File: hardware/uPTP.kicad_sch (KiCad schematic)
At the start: 20 parts, among them J1 Conn_01x04_Pin, J2 PPS_UFL, J3 PPS_SMA, J5 AUX_PWR, U1 CH32V307WCU6, Y1 Crystal_GND2_Small

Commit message: Done for the day
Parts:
- J1: value Conn_01x04_Pin -> UART_HDR
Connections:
- net GND: now also J1.1 (Pin_1), J5.1 (Pin_1), U1.0 (EP), U1.12 (VSSA), U1.18 (VSS), U1.49 (VSS), U1.69 (VSS)
- net Power/V_AUX: now also J5.2 (Pin_2)
- net UART_TX: now reaches J1.2 (Pin_2)
- net UART_RX: now reaches J1.3 (Pin_3)
- net +3V3: now reaches J1.4 (Pin_4)
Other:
- moved on the sheet: J1, J5

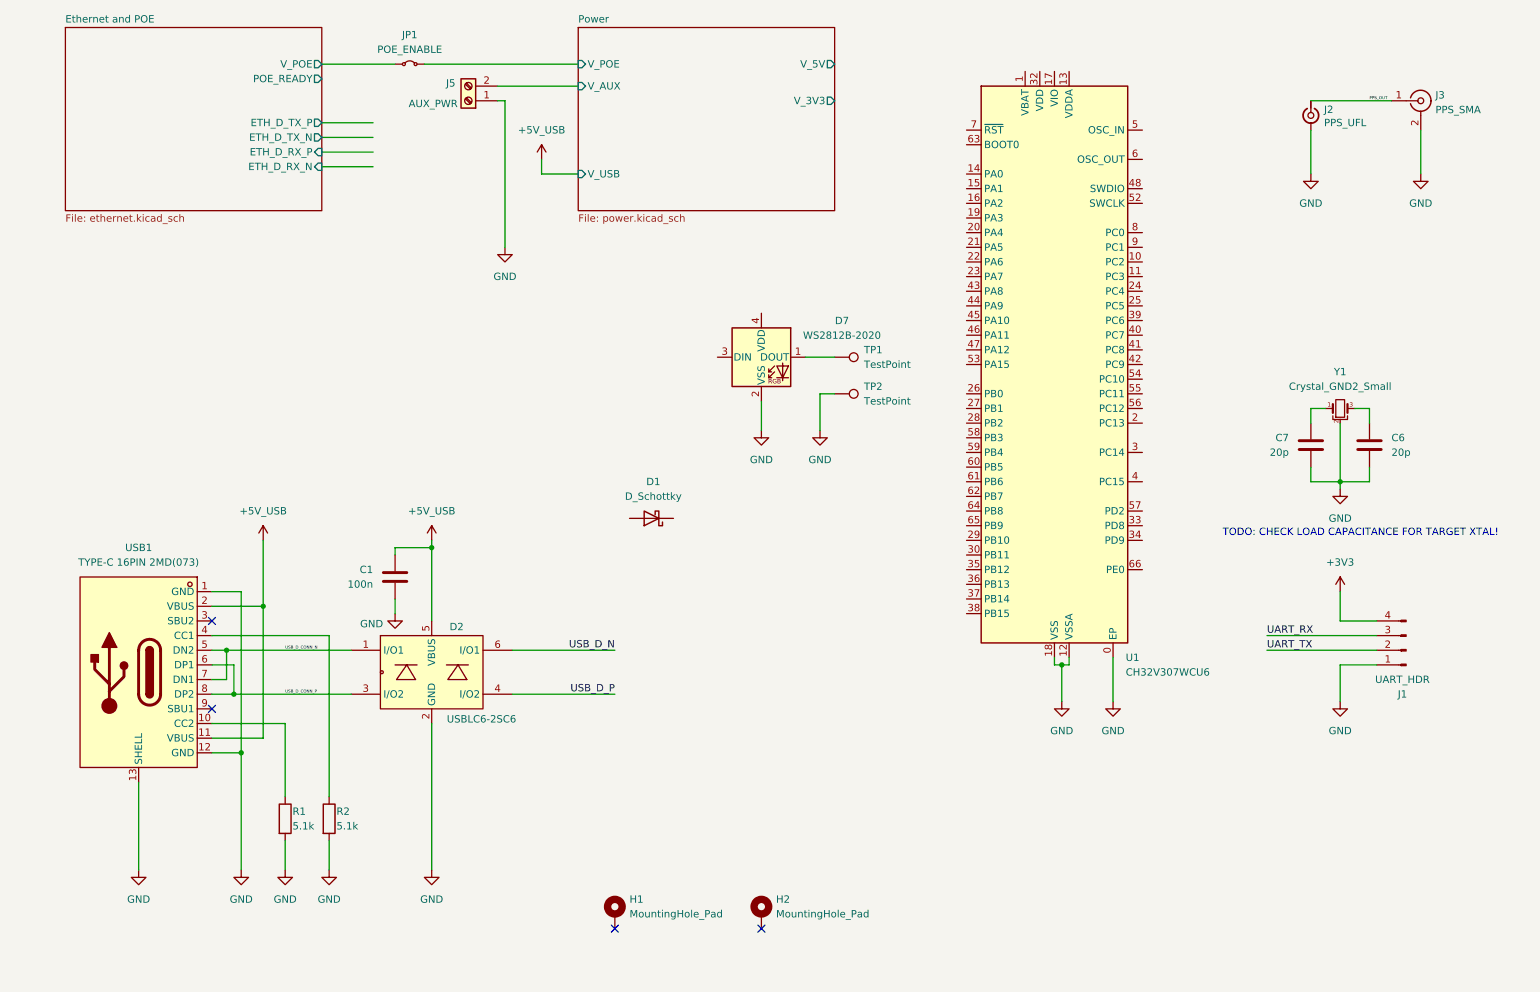
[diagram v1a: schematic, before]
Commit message: Prep for change to SI3404 https://www.skyworksinc.com/-/media/Skyworks/SL/documents/public/application-notes/an1130-si3404-06x-dg.pdf
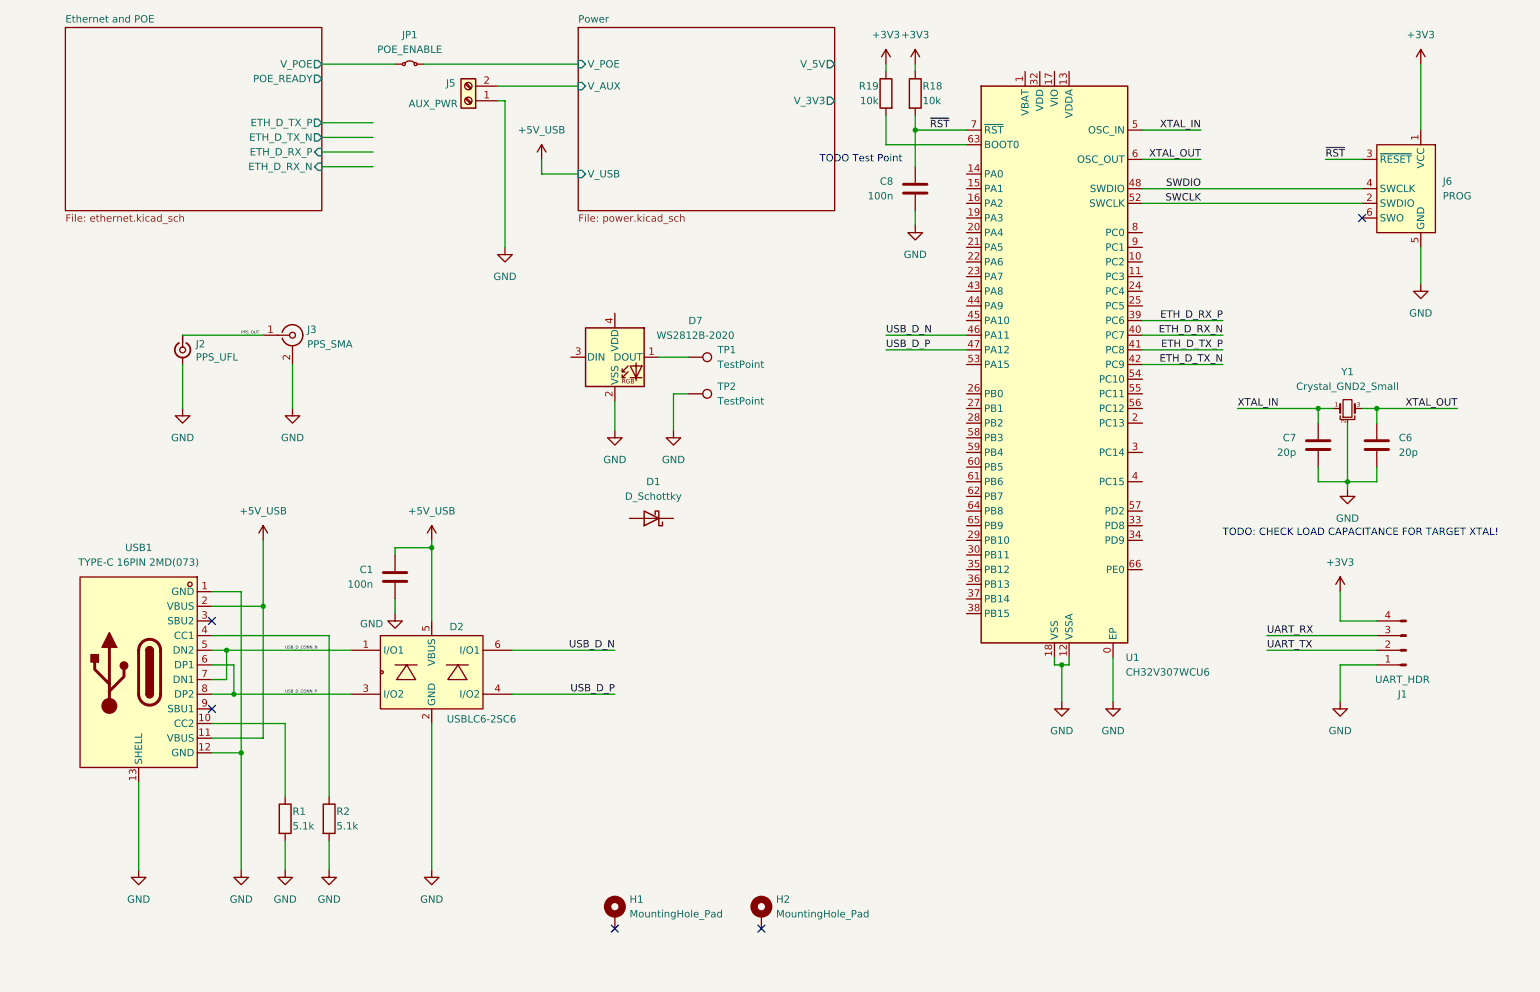
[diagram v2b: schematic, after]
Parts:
- added C8: 100n, Capacitor_SMD:C_0402_1005Metric, symbol Device:C
- added J6: PROG, Connector:Tag-Connect_TC2030-IDC-NL_2x03_P1.27mm_Vertical, symbol Connector:Conn_ARM_SWD_TagConnect_TC2030-NL
- added R18, R19: 10k, Resistor_SMD:R_0402_1005Metric, symbol Device:R
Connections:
- net +3V3: now also J6.1 (VCC), R18.1, R19.1
- net GND: now also C8.2, J6.5 (GND)
- net USB_D_N: now also U1.46 (PA11)
- net USB_D_P: now also U1.47 (PA12)
- net XTAL_OUT: now reaches C6.1, Y1.3
- net XTAL_OUT: now also U1.6 (OSC_OUT)
- net XTAL_IN: now reaches C7.1, Y1.1
- net XTAL_IN: now also U1.5 (OSC_IN)
- net ETH_D_RX_P: now reaches U1.39 (PC6)
- net ETH_D_RX_N: now reaches U1.40 (PC7)
- net ETH_D_TX_P: now reaches U1.41 (PC8)
- net ETH_D_TX_N: now reaches U1.42 (PC9)
- net SWDIO: now reaches U1.48 (SWDIO)
- net SWDIO: now also J6.4 (SWCLK)
- net SWCLK: now reaches U1.52 (SWCLK)
- net SWCLK: now also J6.2 (SWDIO)
- net at U1.63 (BOOT0): now also R19.2
- net ~{RST}: now reaches U1.7 (~{RST})
- net ~{RST}: now also C8.1, J6.3 (~{RESET}), R18.2
- no-connect marks 4 -> 5
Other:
- note added: "TODO Test Point"
- moved on the sheet: C6, C7, D7, J2, J3, TP1, TP2, Y1

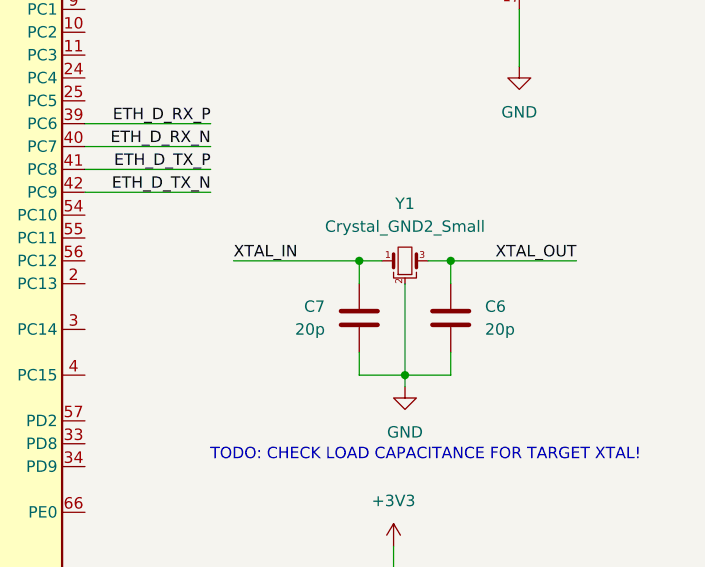
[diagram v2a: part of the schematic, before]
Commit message: Add XTAL, rough POE Schematic
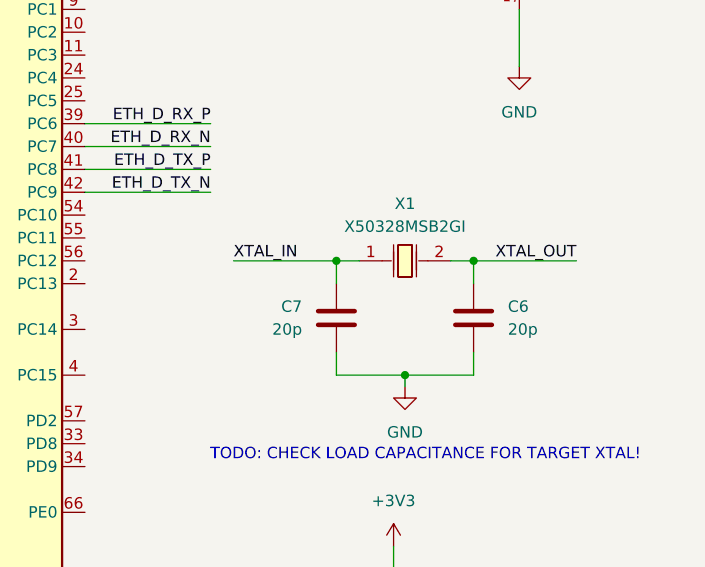
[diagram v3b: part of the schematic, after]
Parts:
- removed Y1: Crystal_GND2_Small, symbol Device:Crystal_GND2_Small
- added X1: X50328MSB2GI, uPTP:CRYSTAL-SMD_L5.0-W3.2, symbol uPTP:X50328MSB2GI
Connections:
- net XTAL_IN: now also X1.1
- net XTAL_OUT: now also X1.2
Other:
- moved on the sheet: C6, C7
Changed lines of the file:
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@@
-	)
-	(junction
-		(at 259.08 97.79)
-		(diameter 0)
-		(color 0 0 0 0)
 	)
 	(junction
@@
 	)
 	(junction
-		(at 248.92 97.79)
+		(at 261.62 97.79)
+		(diameter 0)
+		(color 0 0 0 0)
+	)
+	(junction
+		(at 246.38 97.79)
 		(diameter 0)
 		(color 0 0 0 0)
@@
 	(wire
 		(pts
-			(xy 254 110.49) (xy 248.92 110.49)
+			(xy 254 110.49) (xy 246.38 110.49)
+		)
+		(stroke
+			(width 0)
+			(type default)
+		)
+	)
+	(wire
+		(pts
+			(xy 246.38 97.79) (xy 248.92 97.79)
 		)
 		(stroke
@@
 	(wire
 		(pts
+			(xy 261.62 97.79) (xy 273.05 97.79)
+		)
+		(stroke
+			(width 0)
+			(type default)
+		)
+	)
+	(wire
+		(pts
 			(xy 179.07 63.5) (xy 179.07 66.04)
 		)
@@
 	(wire
 		(pts
-			(xy 259.08 110.49) (xy 254 110.49)
+			(xy 261.62 110.49) (xy 254 110.49)
 		)
 		(stroke
@@
 	(wire
 		(pts
+			(xy 259.08 97.79) (xy 261.62 97.79)
+		)
+		(stroke
+			(width 0)
+			(type default)
+		)
+	)
+	(wire
+		(pts
 			(xy 106.68 41.91) (xy 120.65 41.91)
 		)
@@
 	(wire
 		(pts
-			(xy 248.92 97.79) (xy 248.92 100.33)
+			(xy 246.38 97.79) (xy 246.38 100.33)
 		)
 		(stroke
@@
 	(wire
 		(pts
-			(xy 254 100.33) (xy 254 110.49)
-		)
-		(stroke
-			(width 0)
-			(type default)
-		)
-	)
-	(wire
-		(pts
 			(xy 57.15 129.54) (xy 62.23 129.54)
 		)
@@
 	(wire
 		(pts
-			(xy 259.08 97.79) (xy 273.05 97.79)
-		)
-		(stroke
-			(width 0)
-			(type default)
-		)
-	)
-	(wire
-		(pts
 			(xy 59.69 139.7) (xy 59.69 144.78)
 		)
@@
 	(wire
 		(pts
-			(xy 256.54 97.79) (xy 259.08 97.79)
-		)
-		(stroke
-			(width 0)
-			(type default)
-		)
-	)
-	(wire
-		(pts
 			(xy 218.44 85.09) (xy 232.41 85.09)
 		)
@@
 	(wire
 		(pts
-			(xy 234.95 97.79) (xy 248.92 97.79)
+			(xy 234.95 97.79) (xy 246.38 97.79)
 		)
 		(stroke
@@
 	(wire
 		(pts
-			(xy 259.08 107.95) (xy 259.08 110.49)
-		)
-		(stroke
-			(width 0)
-			(type default)
-		)
-	)
-	(wire
-		(pts
-			(xy 251.46 97.79) (xy 248.92 97.79)
+			(xy 261.62 107.95) (xy 261.62 110.49)
 		)
 		(stroke
@@
 	(wire
 		(pts
-			(xy 259.08 100.33) (xy 259.08 97.79)
+			(xy 261.62 100.33) (xy 261.62 97.79)
 		)
 		(stroke
@@
 	(wire
 		(pts
-			(xy 248.92 110.49) (xy 248.92 107.95)
+			(xy 246.38 110.49) (xy 246.38 107.95)
 		)
 		(stroke
@@
 	(symbol
 		(lib_id "Device:C")
-		(at 259.08 104.14 0)
+		(at 261.62 104.14 0)
 		(unit 1)
 		(exclude_from_sim no)
@@
 		(dnp no)
 		(property "Reference" "C6"
-			(at 262.89 102.8699 0)
+			(at 265.43 102.8699 0)
 			(effects
 				(font
@@
 		)
 		(property "Value" "20p"
-			(at 262.89 105.4099 0)
+			(at 265.43 105.4099 0)
 			(effects
 				(font
@@
 		)
 		(property "Footprint" "Capacitor_SMD:C_0402_1005Metric"
-			(at 260.0452 107.95 0)
+			(at 262.5852 107.95 0)
 			(effects
 				(font
@@
 		)
 		(property "Datasheet" "~"
-			(at 259.08 104.14 0)
+			(at 261.62 104.14 0)
 			(effects
 				(font
@@
 		)
 		(property "Description" "Unpolarized capacitor"
-			(at 259.08 104.14 0)
+			(at 261.62 104.14 0)
 			(effects
 				(font
@@
 	)
 	(symbol
-		(lib_id "Device:Crystal_GND2_Small")
-		(at 254 97.79 0)
-		(unit 1)
-		(exclude_from_sim no)
-		(in_bom yes)
-		(on_board yes)
-		(dnp no)
-		(fields_autoplaced yes)
-		(property "Reference" "Y1"
-			(at 254 91.44 0)
-			(effects
-				(font
-					(size 1.27 1.27)
-				)
-			)
-		)
-		(property "Value" "Crystal_GND2_Small"
-			(at 254 93.98 0)
-			(effects
-				(font
-					(size 1.27 1.27)
-				)
-			)
-		)
-		(property "Footprint" ""
-			(at 254 97.79 0)
-			(effects
-				(font
-					(size 1.27 1.27)
-				)
-				(hide yes)
-			)
-		)
-		(property "Datasheet" "~"
-			(at 254 97.79 0)
-			(effects
-				(font
-					(size 1.27 1.27)
-				)
-				(hide yes)
-			)
-		)
-		(property "Description" "Three pin crystal, GND on pin 2, small symbol"
-			(at 254 97.79 0)
-			(effects
-				(font
-					(size 1.27 1.27)
-				)
-				(hide yes)
-			)
-		)
-		(pin "2"
-		)
-		(pin "3"
-		)
-		(pin "1"
-		)
-		(instances
-			(project ""
-				(path "/c29659fd-9e8d-4714-a690-4e74e6e849c2"
-					(reference "Y1")
-					(unit 1)
-				)
-			)
-		)
-	)
-	(symbol
 		(lib_id "Device:C")
 		(at 179.07 59.69 0)
@@
 	)
 	(symbol
+		(lib_id "uPTP:X50328MSB2GI")
+		(at 254 97.79 0)
+		(unit 1)
+		(exclude_from_sim no)
+		(in_bom yes)
+		(on_board yes)
+		(dnp no)
+		(fields_autoplaced yes)
+		(property "Reference" "X1"
+			(at 254 91.44 0)
+			(effects
+				(font
+					(size 1.27 1.27)
+				)
+			)
+		)
+		(property "Value" "X50328MSB2GI"
+			(at 254 93.98 0)
+			(effects
+				(font
+					(size 1.27 1.27)
+				)
+			)
+		)
+		(property "Footprint" "uPTP:CRYSTAL-SMD_L5.0-W3.2"
+			(at 254 105.41 0)
+			(effects
+				(font
+					(size 1.27 1.27)
+				)
+				(hide yes)
+			)
+		)
+		(property "Datasheet" "https://lcsc.com/product-detail/SMD-Crystals_YSX530GA-8MHZ-20PF-10PPM-40-85_C115962.html"
+			(at 254 107.95 0)
+			(effects
+				(font
+					(size 1.27 1.27)
+				)
+				(hide yes)
+			)
+		)
+		(property "Description" "8MHz Crystal Oscillator (Basic Part)"
+			(at 255.27 112.776 0)
+			(effects
+				(font
+					(size 1.27 1.27)
+				)
+				(hide yes)
+			)
+		)
+		(property "LCSC Part" "C115962"
+			(at 254 110.49 0)
+			(effects
+				(font
+					(size 1.27 1.27)
+				)
+				(hide yes)
+			)
+		)
+		(pin "1"
+		)
+		(pin "2"
+		)
+		(instances
+			(project ""
+				(path "/c29659fd-9e8d-4714-a690-4e74e6e849c2"
+					(reference "X1")
+					(unit 1)
+				)
+			)
+		)
+	)
+	(symbol
 		(lib_id "power:+5VD")
 		(at 95.25 120.65 0)
@@
 	(symbol
 		(lib_id "Device:C")
-		(at 248.92 104.14 0)
+		(at 246.38 104.14 0)
 		(mirror y)
 		(unit 1)
@@
 		(dnp no)
 		(property "Reference" "C7"
-			(at 245.11 102.8699 0)
+			(at 242.57 102.8699 0)
 			(effects
 				(font
@@
 		)
 		(property "Value" "20p"
-			(at 245.11 105.4099 0)
+			(at 242.57 105.4099 0)
 			(effects
 				(font
@@
 		)
 		(property "Footprint" "Capacitor_SMD:C_0402_1005Metric"
-			(at 247.9548 107.95 0)
+			(at 245.4148 107.95 0)
 			(effects
 				(font
@@
 		)
 		(property "Datasheet" "~"
-			(at 248.92 104.14 0)
+			(at 246.38 104.14 0)
 			(effects
 				(font
@@
 		)
 		(property "Description" "Unpolarized capacitor"
-			(at 248.92 104.14 0)
-			(effects
-				(font
+			(at 246.38 104.14 0)
+			(effects
+				(font
